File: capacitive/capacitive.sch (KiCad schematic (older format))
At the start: 54 parts, among them J101 I2C, J102 UART, J103 SWD, U101 STM32F070C6T6, U102 TLV9062IDR

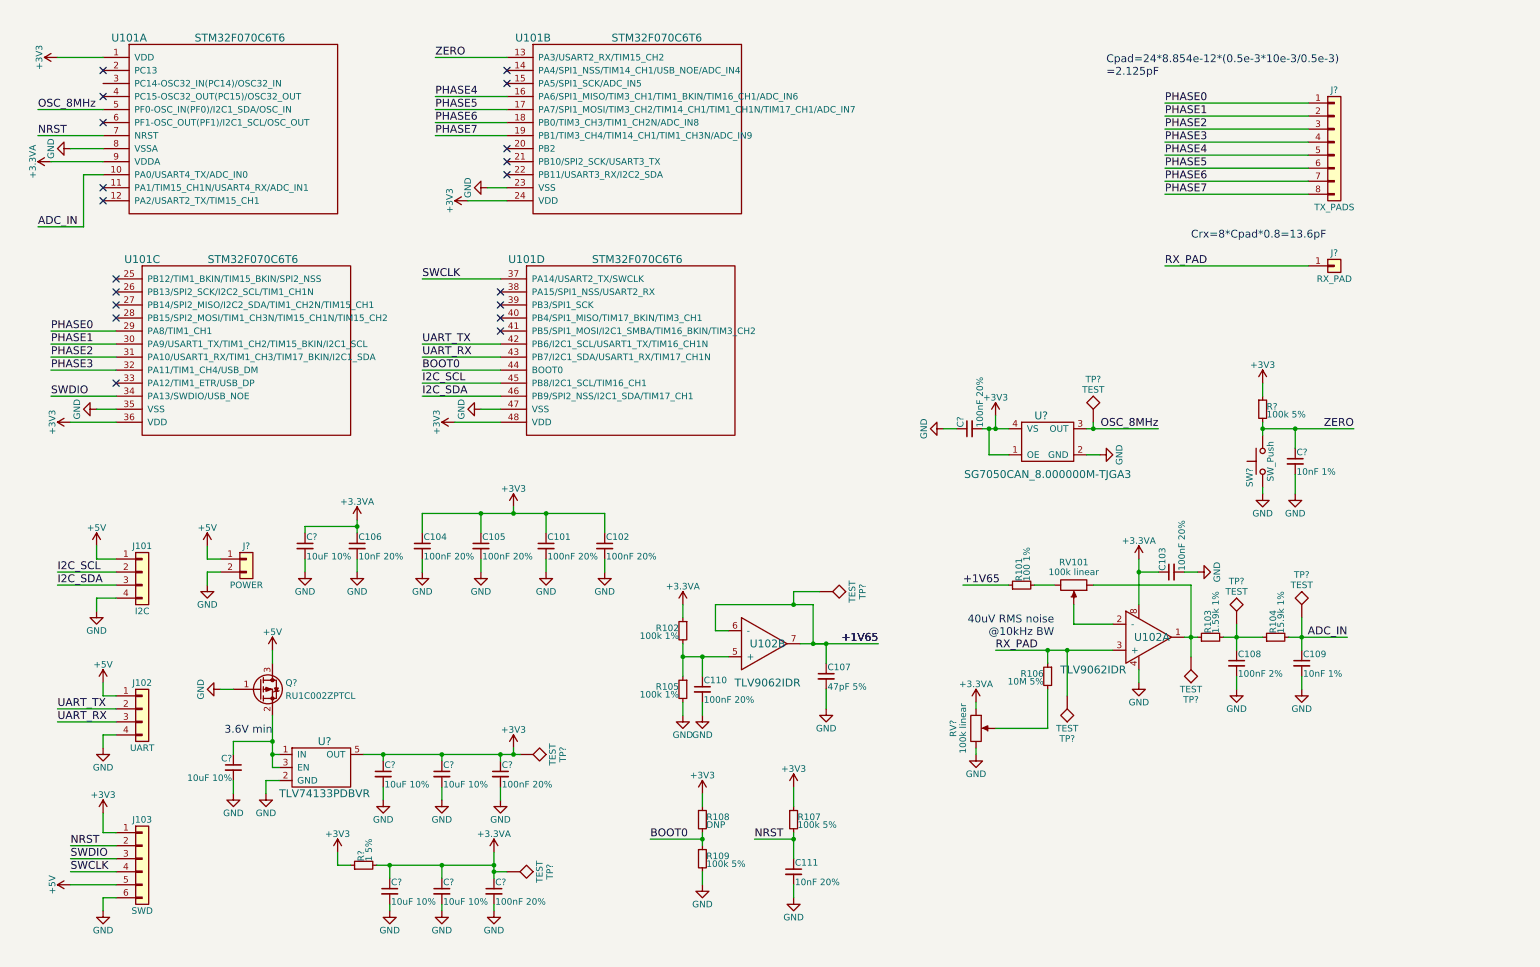
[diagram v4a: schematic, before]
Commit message: Add some footprints
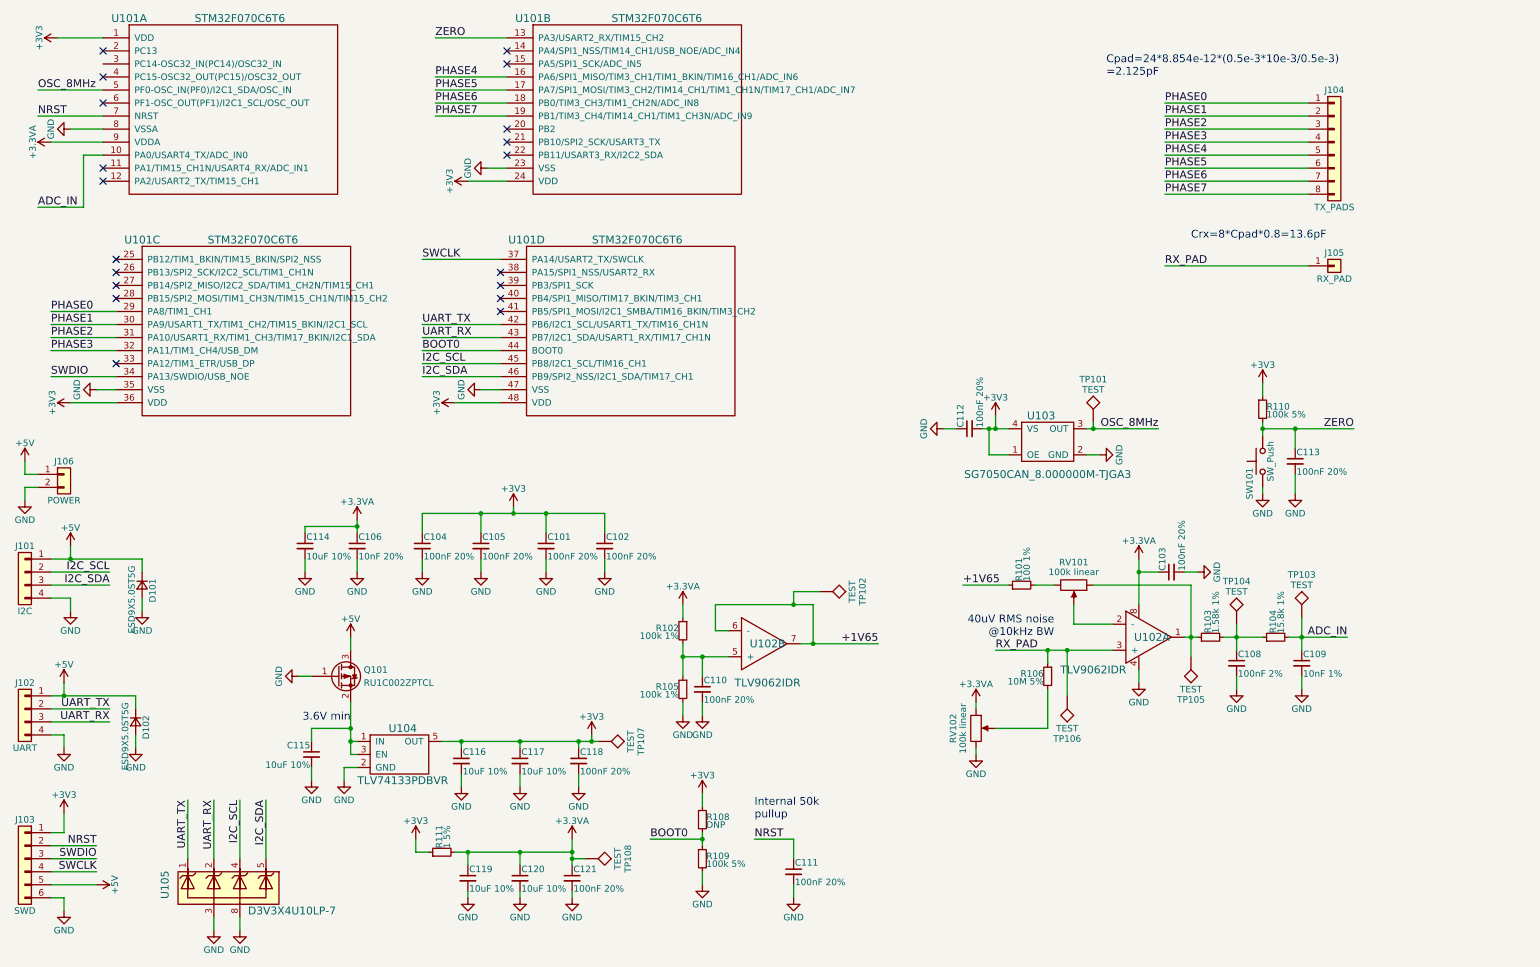
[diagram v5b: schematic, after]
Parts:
- removed C107: 47pF 5%, symbol C_Small
- removed R107: 100k 5%, symbol R_Small
- added D101, D102: ESD9X5.0ST5G, capacitive:SOD-923, symbol D_Small
- added U105: D3V3X4U10LP-7, capacitive:Diode_U-DFN2510-10, symbol D3V3X4U10LP-7
- C108: footprint (none) -> Capacitors_SMD:C_1210_HandSoldering; Mouser (none) -> 667-ECH-U1C104GX5
- C109: footprint (none) -> Capacitors_SMD:C_0805_HandSoldering; Mouser (none) -> 81-GRM2195C1H103FA1D
- C111: value 10nF 20% -> 100nF 20%
- C113: renamed from C?; value 10nF 1% -> 100nF 20%
- J101, J102: footprint (none) -> Socket_Strips:Socket_Strip_Straight_1x04_Pitch2.54mm
- J103: footprint (none) -> Socket_Strips:Socket_Strip_Straight_2x03_Pitch2.54mm
- J106: renamed from J?; footprint (none) -> Socket_Strips:Socket_Strip_Straight_1x02_Pitch2.54mm
- Q101: renamed from Q?; footprint (none) -> capacitive:Rohm_UMT3F
- R101: footprint (none) -> Resistors_SMD:R_0603_HandSoldering; Mouser (none) -> 71-CRCW0603100RFKEAC
- R103: value 1.59k 1% -> 1.58k 1%; footprint (none) -> Resistors_SMD:R_0603_HandSoldering; Mouser (none) -> 660-RN73H1JTD1581D25
- R104: value 15.9k 1% -> 15.8k 1%; footprint (none) -> Resistors_SMD:R_1206_HandSoldering; Mouser (none) -> ERJ-8ENF1582V
- R106: footprint (none) -> Resistors_SMD:R_0603_HandSoldering; Mouser (none) -> 652-CR0603JW-106ELF
- R108: footprint (none) -> Resistors_SMD:R_0603_HandSoldering
- R111: renamed from R?; footprint (none) -> Resistors_SMD:R_0603_HandSoldering; Mouser (none) -> 755-ESR03EZPJ1R0
- TP102: renamed from TP?; footprint (none) -> Measurement_Points:Measurement_Point_Round-SMD-Pad_Small
- U101: footprint (none) -> capacitive:ST_LQFP48
- U103: renamed from U?; footprint (none) -> Crystals:Crystal_SMD_7050-4pin_7.0x5.0mm
- U104: renamed from U?; footprint (none) -> TO_SOT_Packages_SMD:SOT-23-5_HandSoldering
- gave numbers to parts that had none: 21
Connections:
- net +5V: now also D101.1 (K), D102.1 (K)
- net GND: now also D101.2 (A), D102.2 (A), U105.3 (GND), U105.8 (GND)
- net I2C_SCL: now also U105.4 (K3)
- net I2C_SDA: now also U105.5 (K4)
- net UART_RX: now also U105.2 (K2)
- net UART_TX: now also U105.1 (K1)
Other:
- note added: "Internal 50k\npullup"
- moved on the sheet: C115, C116, C117, C118, C119, C120, C121, J101, J102, J103, J106, Q101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

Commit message: Generate TI SOIC-8 footprint
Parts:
- C106: value 10nF 20% -> 10nF 10%; footprint (none) -> Resistors_SMD:R_0603_HandSoldering; Mouser (none) -> VJ0603Y103KXAAC
- R102: footprint (none) -> Resistors_SMD:R_1206_HandSoldering; Mouser (none) -> 71-CRCW1206100KFKEAC
- R109, R110: value 100k 5% -> 100k 1%
- RV101: Mouser (none) -> 72-T70YE-100K
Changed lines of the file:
@@
 F 0 "R102" H 5730 5320 50  0000 L CNN
 F 1 "100k 1%" H 5730 5260 50  0000 L CNN
-F 2 "" H 5700 5300 50  0001 C CNN
+F 2 "Resistors_SMD:R_1206_HandSoldering" H 5700 5300 50  0001 C CNN
 F 3 "" H 5700 5300 50  0001 C CNN
+F 4 "71-CRCW1206100KFKEAC" H 5700 5300 60  0001 C CNN "Mouser"
 	1    5700 5300
 	-1   0    0    -1
@@
 P 3200 4650
 F 0 "C106" H 3210 4720 50  0000 L CNN
-F 1 "10nF 20%" H 3210 4570 50  0000 L CNN
-F 2 "" H 3200 4650 50  0001 C CNN
+F 1 "10nF 10%" H 3210 4570 50  0000 L CNN
+F 2 "Resistors_SMD:R_0603_HandSoldering" H 3200 4650 50  0001 C CNN
 F 3 "" H 3200 4650 50  0001 C CNN
+F 4 "VJ0603Y103KXAAC" H 3200 4650 60  0001 C CNN "Mouser"
 	1    3200 4650
 	1    0    0    -1
@@
 F 2 "" H 8700 4950 50  0001 C CNN
 F 3 "" H 8700 4950 50  0001 C CNN
+F 4 "72-T70YE-100K" V 8700 4950 60  0001 C CNN "Mouser"
 	1    8700 4950
 	0    1    1    0
@@
 P 5850 7050
 F 0 "R109" H 5880 7070 50  0000 L CNN
-F 1 "100k 5%" H 5880 7010 50  0000 L CNN
+F 1 "100k 1%" H 5880 7010 50  0000 L CNN
 F 2 "" H 5850 7050 50  0001 C CNN
 F 3 "" H 5850 7050 50  0001 C CNN
@@
 P 10150 3600
 F 0 "R110" H 10180 3620 50  0000 L CNN
-F 1 "100k 5%" H 10180 3560 50  0000 L CNN
+F 1 "100k 1%" H 10180 3560 50  0000 L CNN
 F 2 "" H 10150 3600 50  0001 C CNN
 F 3 "" H 10150 3600 50  0001 C CNN

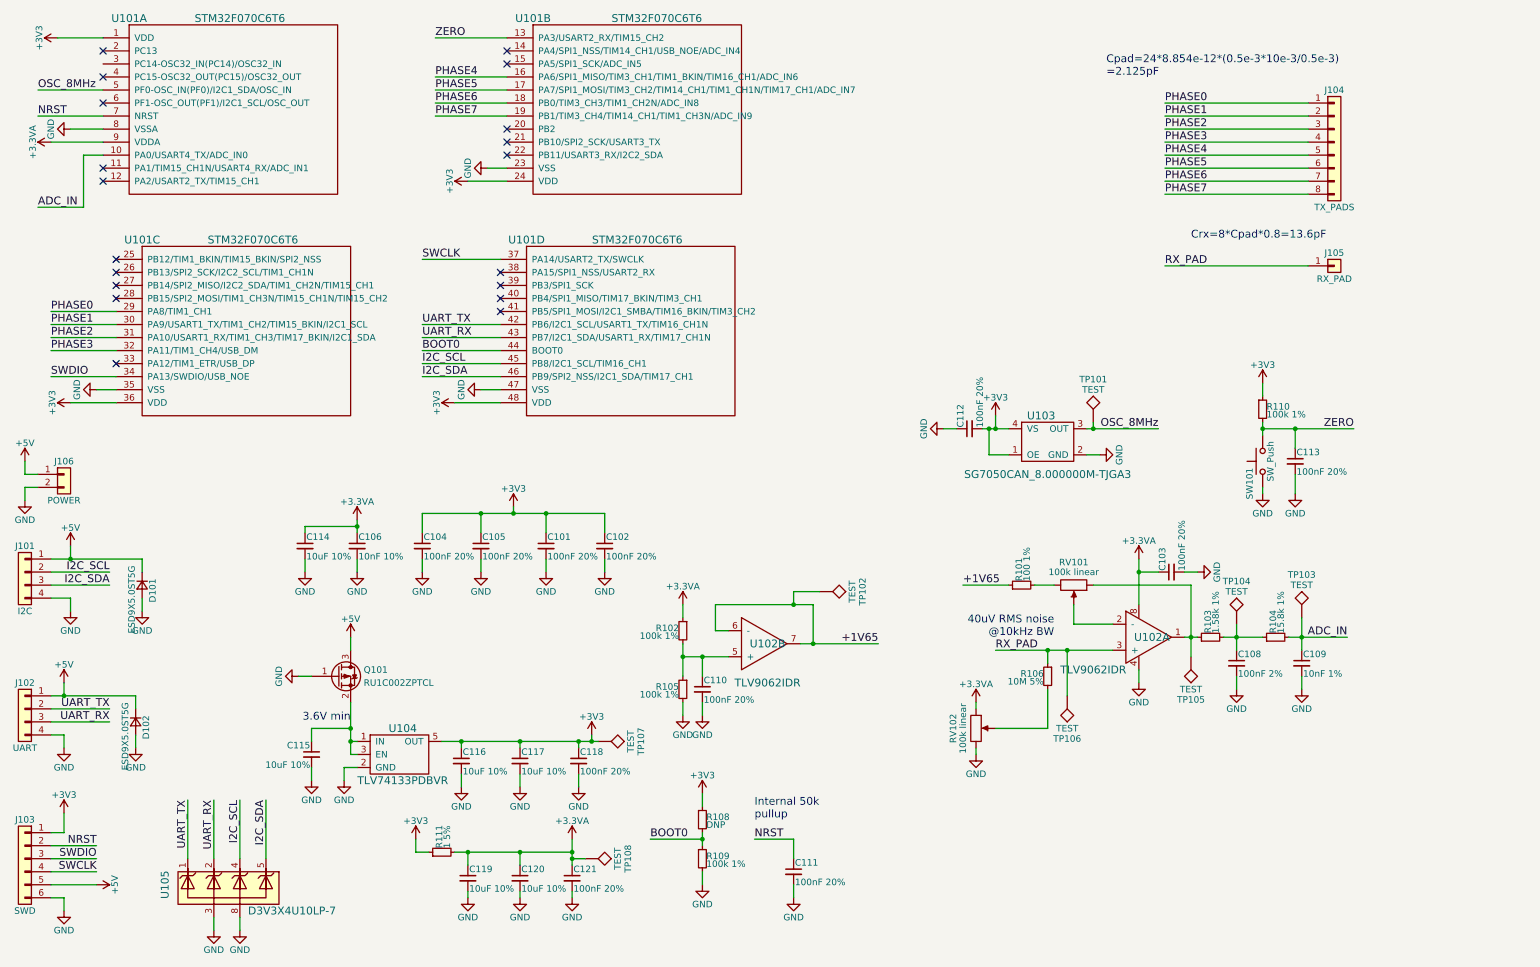
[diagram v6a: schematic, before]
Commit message: Everything footprinted except for the scale coupling pads
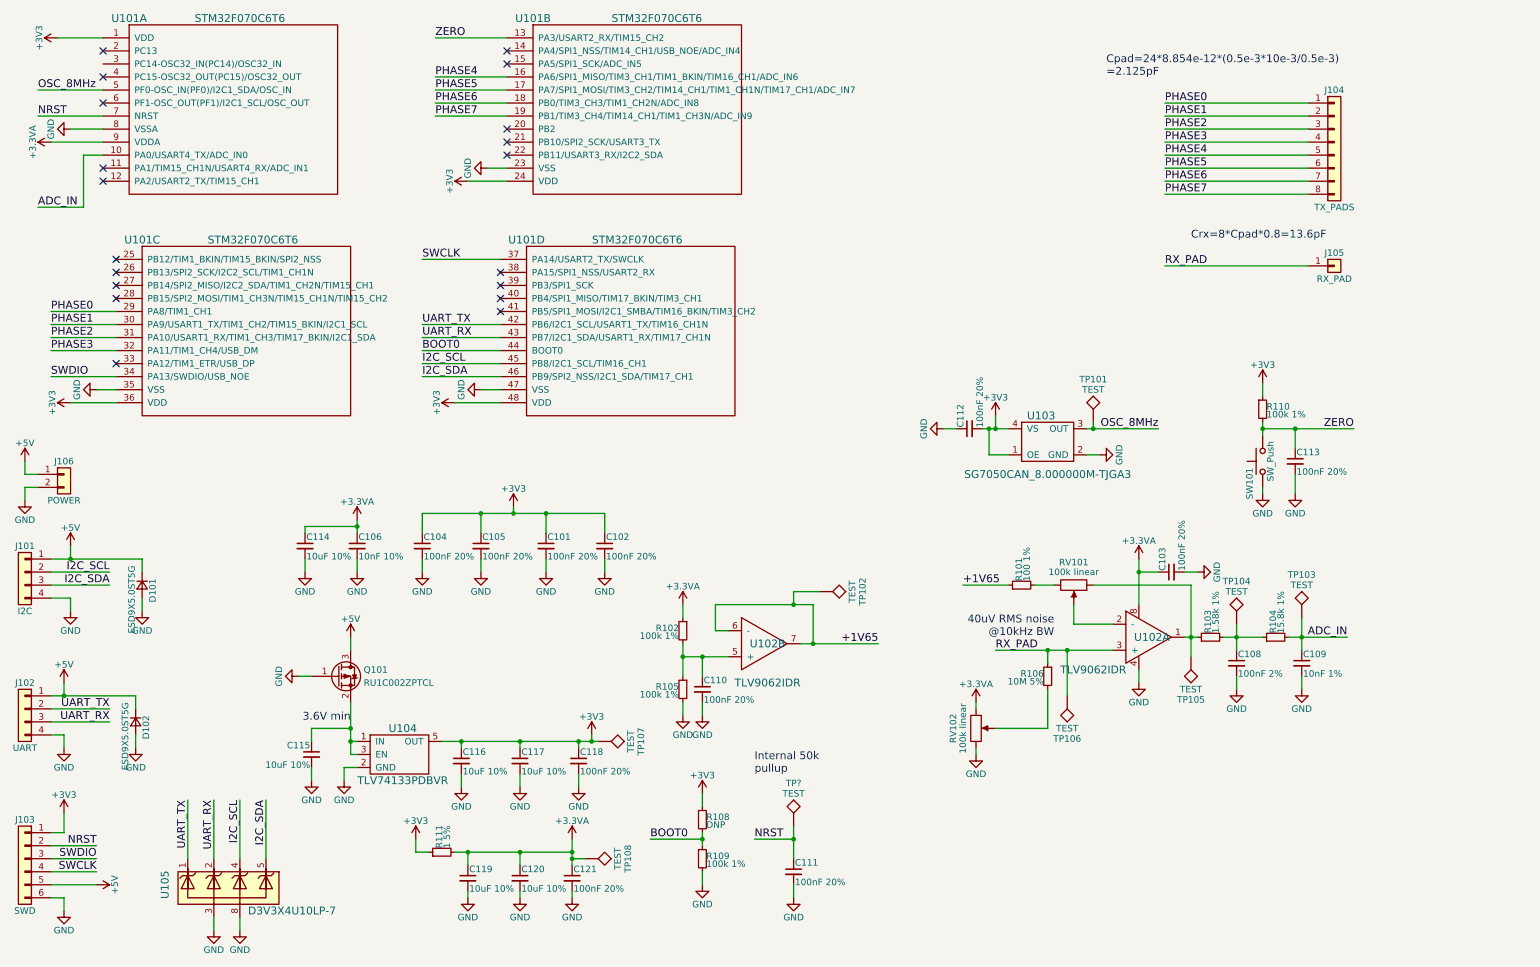
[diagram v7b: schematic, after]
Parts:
- added TP?: TEST, Measurement_Points:Measurement_Point_Round-SMD-Pad_Small, symbol TEST
- J101, J102: Mouser (none) -> 855-M20-9990445
- J103, J104, J105, J106, TP102: Mouser (none) -> NoPart
- RV101: footprint (none) -> capacitive:Vishay_T73YE
- SW101: footprint (none) -> capacitive:LL3301NF065QG; Mouser (none) -> 612-LL3301NF065QG
- U102: footprint (none) -> capacitive:TI_SOIC-8
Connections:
- net NRST: now also TP?.1

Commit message: Autofill components
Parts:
- C111, C113: footprint (none) -> Capacitors_SMD:C_0805_HandSoldering; Mouser (none) -> 710-885012207016
- D102: Mouser (none) -> 863-ESD9X5.0ST5G
- R105, R109, R110: footprint (none) -> Resistors_SMD:R_1206_HandSoldering; Mouser (none) -> 71-CRCW1206100KFKEAC
- RV102: footprint (none) -> capacitive:Vishay_T73YE; Mouser (none) -> 72-T70YE-100K
- TP101, TP103, TP104, TP105, TP106, TP107, TP108: footprint (none) -> Measurement_Points:Measurement_Point_Round-SMD-Pad_Small; Mouser (none) -> NoPart
- U101: Mouser (none) -> 511-STM32F070C6T6
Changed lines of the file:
@@
 F 2 "capacitive:ST_LQFP48" H 1450 600 60  0001 C CNN
 F 3 "" H 1450 600 60  0001 C CNN
+F 4 "511-STM32F070C6T6" H 1450 600 60  0001 C "Mouser"
 	1    1450 600
 	1    0    0    -1
@@
 F 2 "capacitive:ST_LQFP48" H 4550 600 60  0001 C CNN
 F 3 "" H 4550 600 60  0001 C CNN
+F 4 "511-STM32F070C6T6" H 4550 600 60  0001 C "Mouser"
 	2    4550 600
 	1    0    0    -1
@@
 F 2 "capacitive:ST_LQFP48" H 4500 2300 60  0001 C CNN
 F 3 "" H 4500 2300 60  0001 C CNN
+F 4 "511-STM32F070C6T6" H 4500 2300 60  0001 C "Mouser"
 	4    4500 2300
 	1    0    0    -1
@@
 F 0 "C111" H 6560 7220 50  0000 L CNN
 F 1 "100nF 20%" H 6560 7070 50  0000 L CNN
-F 2 "" H 6550 7150 50  0001 C CNN
+F 2 "Capacitors_SMD:C_0805_HandSoldering" H 6550 7150 50  0001 C CNN
 F 3 "" H 6550 7150 50  0001 C CNN
+F 4 "710-885012207016" H 6550 7150 50  0001 C "Mouser"
 	1    6550 7150
 	1    0    0    -1
@@
 F 0 "R105" H 5730 5770 50  0000 L CNN
 F 1 "100k 1%" H 5730 5710 50  0000 L CNN
-F 2 "" H 5700 5750 50  0001 C CNN
+F 2 "Resistors_SMD:R_1206_HandSoldering" H 5700 5750 50  0001 C CNN
 F 3 "" H 5700 5750 50  0001 C CNN
+F 4 "71-CRCW1206100KFKEAC" H 5700 5750 50  0001 C "Mouser"
 	1    5700 5750
 	-1   0    0    -1
@@
 F 0 "R109" H 5880 7070 50  0000 L CNN
 F 1 "100k 1%" H 5880 7010 50  0000 L CNN
-F 2 "" H 5850 7050 50  0001 C CNN
+F 2 "Resistors_SMD:R_1206_HandSoldering" H 5850 7050 50  0001 C CNN
 F 3 "" H 5850 7050 50  0001 C CNN
+F 4 "71-CRCW1206100KFKEAC" H 5850 7050 50  0001 C "Mouser"
 	1    5850 7050
 	1    0    0    -1
@@
 F 0 "TP108" H 4950 7350 50  0000 C BNN
 F 1 "TEST" H 4950 7300 50  0000 C CNN
-F 2 "" H 4950 7050 50  0001 C CNN
+F 2 "Measurement_Points:Measurement_Point_Round-SMD-Pad_Small" H 4950 7050 50  0001 C CNN
 F 3 "" H 4950 7050 50  0001 C CNN
+F 4 "NoPart" H 4950 7050 50  0001 C "Mouser"
 	1    4950 7050
 	0    1    1    0
@@
 F 0 "TP107" H 5050 6450 50  0000 C BNN
 F 1 "TEST" H 5050 6400 50  0000 C CNN
-F 2 "" H 5050 6150 50  0001 C CNN
+F 2 "Measurement_Points:Measurement_Point_Round-SMD-Pad_Small" H 5050 6150 50  0001 C CNN
 F 3 "" H 5050 6150 50  0001 C CNN
+F 4 "NoPart" H 5050 6150 50  0001 C "Mouser"
 	1    5050 6150
 	0    1    1    0
@@
 F 0 "TP106" H 8650 6100 50  0000 C BNN
 F 1 "TEST" H 8650 6050 50  0000 C CNN
-F 2 "" H 8650 5800 50  0001 C CNN
+F 2 "Measurement_Points:Measurement_Point_Round-SMD-Pad_Small" H 8650 5800 50  0001 C CNN
 F 3 "" H 8650 5800 50  0001 C CNN
+F 4 "NoPart" H 8650 5800 50  0001 C "Mouser"
 	1    8650 5800
 	-1   0    0    1
@@
 F 0 "TP105" H 9600 5800 50  0000 C BNN
 F 1 "TEST" H 9600 5750 50  0000 C CNN
-F 2 "" H 9600 5500 50  0001 C CNN
+F 2 "Measurement_Points:Measurement_Point_Round-SMD-Pad_Small" H 9600 5500 50  0001 C CNN
 F 3 "" H 9600 5500 50  0001 C CNN
+F 4 "NoPart" H 9600 5500 50  0001 C "Mouser"
 	1    9600 5500
 	-1   0    0    1
@@
 F 0 "TP104" H 9950 5550 50  0000 C BNN
 F 1 "TEST" H 9950 5500 50  0000 C CNN
-F 2 "" H 9950 5250 50  0001 C CNN
+F 2 "Measurement_Points:Measurement_Point_Round-SMD-Pad_Small" H 9950 5250 50  0001 C CNN
 F 3 "" H 9950 5250 50  0001 C CNN
+F 4 "NoPart" H 9950 5250 50  0001 C "Mouser"
 	1    9950 5250
 	1    0    0    -1
@@
 F 0 "TP103" H 10450 5500 50  0000 C BNN
 F 1 "TEST" H 10450 5450 50  0000 C CNN
-F 2 "" H 10450 5200 50  0001 C CNN
+F 2 "Measurement_Points:Measurement_Point_Round-SMD-Pad_Small" H 10450 5200 50  0001 C CNN
 F 3 "" H 10450 5200 50  0001 C CNN
+F 4 "NoPart" H 10450 5200 50  0001 C "Mouser"
 	1    10450 5200
 	1    0    0    -1
@@
 F 0 "TP101" H 8850 4000 50  0000 C BNN
 F 1 "TEST" H 8850 3950 50  0000 C CNN
-F 2 "" H 8850 3700 50  0001 C CNN
+F 2 "Measurement_Points:Measurement_Point_Round-SMD-Pad_Small" H 8850 3700 50  0001 C CNN
 F 3 "" H 8850 3700 50  0001 C CNN
+F 4 "NoPart" H 8850 3700 50  0001 C "Mouser"
 	1    8850 3700
 	1    0    0    -1
@@
 F 0 "R110" H 10180 3620 50  0000 L CNN
 F 1 "100k 1%" H 10180 3560 50  0000 L CNN
-F 2 "" H 10150 3600 50  0001 C CNN
+F 2 "Resistors_SMD:R_1206_HandSoldering" H 10150 3600 50  0001 C CNN
 F 3 "" H 10150 3600 50  0001 C CNN
+F 4 "71-CRCW1206100KFKEAC" H 10150 3600 50  0001 C "Mouser"
 	1    10150 3600
 	1    0    0    -1
@@
 F 0 "C113" H 10410 4070 50  0000 L CNN
 F 1 "100nF 20%" H 10410 3920 50  0000 L CNN
-F 2 "" H 10400 4000 50  0001 C CNN
+F 2 "Capacitors_SMD:C_0805_HandSoldering" H 10400 4000 50  0001 C CNN
 F 3 "" H 10400 4000 50  0001 C CNN
+F 4 "710-885012207016" H 10400 4000 50  0001 C "Mouser"
 	1    10400 4000
 	1    0    0    -1
@@
 F 0 "RV102" V 7775 6050 50  0000 C CNN
 F 1 "100k linear" V 7850 6050 50  0000 C CNN
-F 2 "" H 7950 6050 50  0001 C CNN
+F 2 "capacitive:Vishay_T73YE" H 7950 6050 50  0001 C CNN
 F 3 "" H 7950 6050 50  0001 C CNN
+F 4 "72-T70YE-100K" H 7950 6050 50  0001 C "Mouser"
 	1    7950 6050
 	1    0    0    -1
@@
 F 2 "capacitive:SOD-923" V 1500 6000 50  0001 C CNN
 F 3 "" V 1500 6000 50  0001 C CNN
+F 4 "863-ESD9X5.0ST5G" V 1500 6000 50  0001 C "Mouser"
 	1    1500 6000
 	0    1    1    0
